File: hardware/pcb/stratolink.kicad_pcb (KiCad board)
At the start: 2 copper layers, 23.4 x 57.3 mm, 61 parts, among them J1 Solar panel direct solder, J2 Solar panel direct solder, J20 Conn_ARM_SWD_TagConnect_TC203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, J3 Conn_PinHeader_1x07_P2.54mm_V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, J4 Conn_PinHeader_1x07_P2.54mm_V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, U2 RAK3172, U5 TMP117NAIYBGR, U7 LIS2DH12TR

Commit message: Refine v1.1 ground zones and local pad connections
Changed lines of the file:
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@@
 			(pintype "power_in")
 			(solder_mask_margin 0)
+			(zone_connect 0)
 		)
 		(pad "6" smd roundrect
@@
 			(pintype "power_in")
 			(solder_mask_margin 0)
+			(zone_connect 0)
 		)
 		(pad "8" smd roundrect
@@
 			(pintype "power_in")
 			(solder_mask_margin 0)
+			(zone_connect 0)
 		)
 		(pad "9" smd roundrect
@@
 			(pinfunction "GND")
 			(pintype "power_in")
+			(zone_connect 2)
 		)
 		(pad "6" connect circle
@@
 			)
 		)
-	)
-	(zone
-		(net "GND")
-		(layer "B.Cu")
-		(hatch edge 0.5)
-		(connect_pads
-			(clearance 0.5)
-		)
-		(min_thickness 0.25)
-		(fill yes
-			(thermal_gap 0.5)
-			(thermal_bridge_width 0.5)
-			(island_removal_mode 0)
-		)
-		(polygon
-			(pts
-				(xy 52.941 29.045069) (xy 76.974 29.136) (xy 76.834 87.152) (xy 52.871 87.502)
-			)
-		)

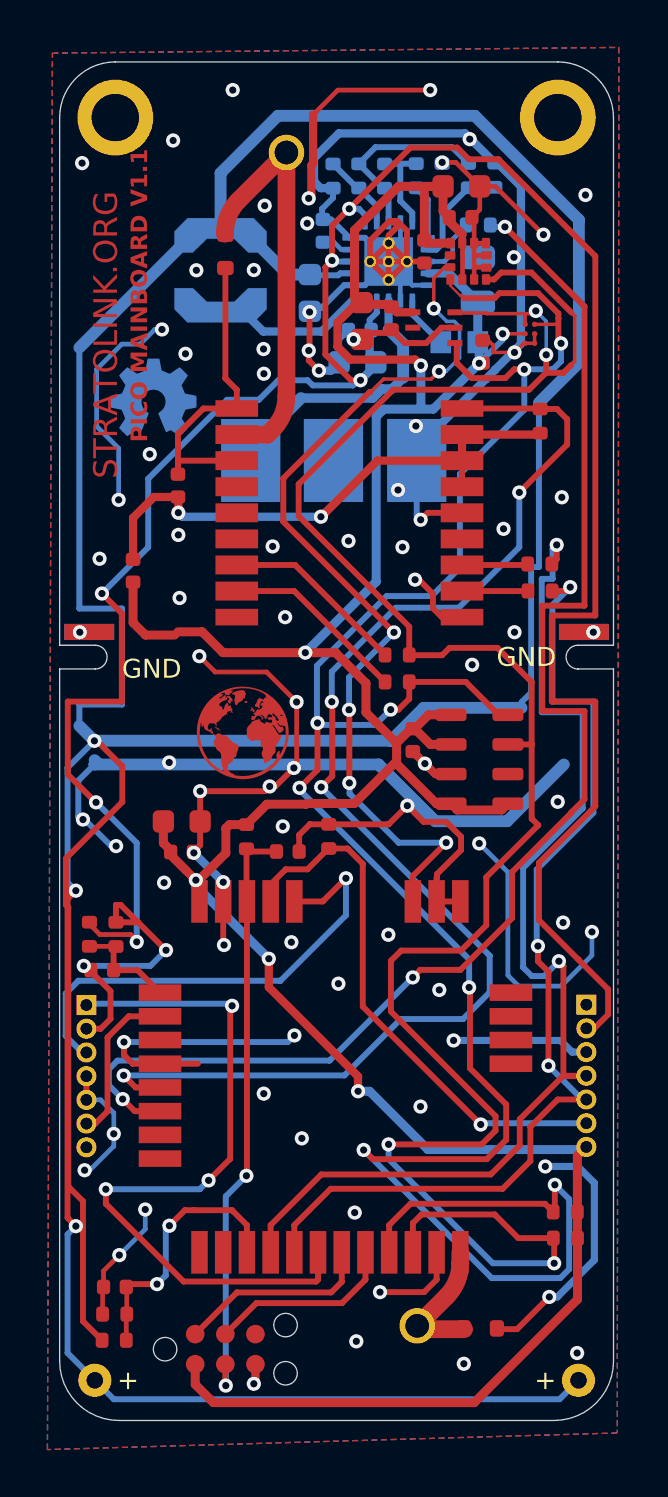
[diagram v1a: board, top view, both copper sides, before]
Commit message: Refine v1.1 edge routing and header pad rings
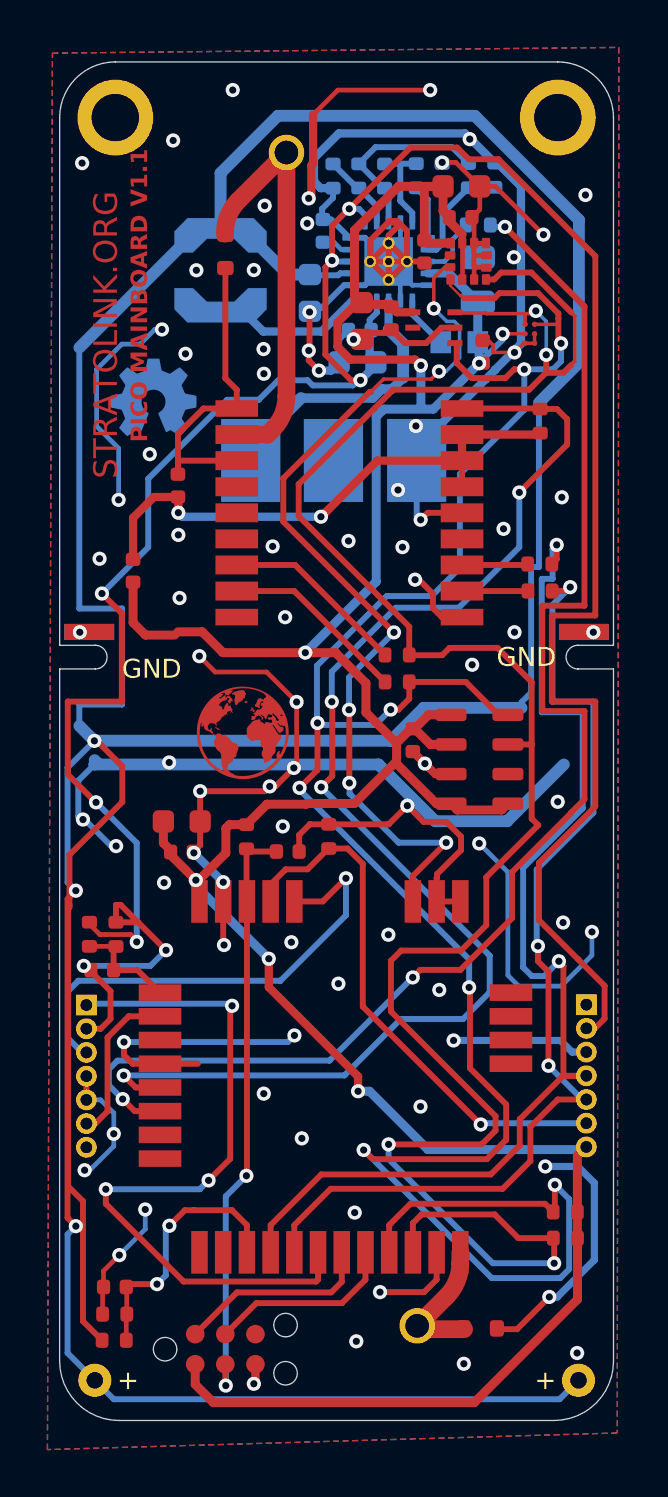
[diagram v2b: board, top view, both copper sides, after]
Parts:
- J3: footprint Connector_PinHeader_1.00mm:PinHeader_1x07_P1.00mm_Vertical -> lib:Stratolink_Header_Left_1x07_P1p00_D0p50_Pad0p88
- J4: footprint Connector_PinHeader_1.00mm:PinHeader_1x07_P1.00mm_Vertical -> lib:Stratolink_Header_Right_1x07_P1p00_D0p50_Pad0p88
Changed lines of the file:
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@@
 		)
 	)
-	(footprint "Connector_PinHeader_1.00mm:PinHeader_1x07_P1.00mm_Vertical"
+	(footprint "lib:Stratolink_Header_Right_1x07_P1p00_D0p50_Pad0p88"
 		(layer "F.Cu")
 		(at 75.531 69.158)
@@
 		(pad "1" thru_hole rect
 			(at 0 0)
-			(size 0.85 0.85)
+			(size 0.88 0.88)
 			(drill 0.5)
 			(layers "*.Cu" "*.Mask")
@@
 		(pad "2" thru_hole oval
 			(at 0 1)
-			(size 0.85 0.85)
+			(size 0.88 0.88)
 			(drill 0.5)
 			(layers "*.Cu" "*.Mask")
@@
 		(pad "3" thru_hole oval
 			(at 0 2)
-			(size 0.85 0.85)
+			(size 0.88 0.88)
 			(drill 0.5)
 			(layers "*.Cu" "*.Mask")
@@
 		(pad "4" thru_hole oval
 			(at 0 3)
-			(size 0.85 0.85)
+			(size 0.88 0.88)
 			(drill 0.5)
 			(layers "*.Cu" "*.Mask")
@@
 		(pad "5" thru_hole oval
 			(at 0 4)
-			(size 0.85 0.85)
+			(size 0.88 0.88)
 			(drill 0.5)
 			(layers "*.Cu" "*.Mask")
@@
 		(pad "6" thru_hole oval
 			(at 0 5)
-			(size 0.85 0.85)
+			(size 0.88 0.88)
 			(drill 0.5)
 			(layers "*.Cu" "*.Mask")
@@
 		(pad "7" thru_hole oval
 			(at 0 6)
-			(size 0.85 0.85)
+			(size 0.88 0.88)
 			(drill 0.5)
 			(layers "*.Cu" "*.Mask")
@@
 		)
 	)
-	(footprint "Connector_PinHeader_1.00mm:PinHeader_1x07_P1.00mm_Vertical"
+	(footprint "lib:Stratolink_Header_Left_1x07_P1p00_D0p50_Pad0p88"
 		(layer "F.Cu")
 		(at 54.444998 69.173998)
@@
 		(pad "1" thru_hole rect
 			(at 0 0)
-			(size 0.85 0.85)
+			(size 0.88 0.88)
 			(drill 0.5)
 			(layers "*.Cu" "*.Mask")
@@
 		(pad "2" thru_hole oval
 			(at 0 1.000001)
-			(size 0.85 0.85)
+			(size 0.88 0.88)
 			(drill 0.5)
 			(layers "*.Cu" "*.Mask")
@@
 		(pad "3" thru_hole oval
 			(at 0.000001 2.000003)
-			(size 0.85 0.85)
+			(size 0.88 0.88)
 			(drill 0.5)
 			(layers "*.Cu" "*.Mask")
@@
 		(pad "4" thru_hole oval
 			(at 0.000002 3.000002)
-			(size 0.85 0.85)
+			(size 0.88 0.88)
 			(drill 0.5)
 			(layers "*.Cu" "*.Mask")
@@
 		(pad "5" thru_hole oval
 			(at 0 4)
-			(size 0.85 0.85)
+			(size 0.88 0.88)
 			(drill 0.5)
 			(layers "*.Cu" "*.Mask")
@@
 		(pad "6" thru_hole oval
 			(at 0 5)
-			(size 0.85 0.85)
+			(size 0.88 0.88)
 			(drill 0.5)
 			(layers "*.Cu" "*.Mask")
@@
 		(pad "7" thru_hole oval
 			(at 0 6)
-			(size 0.85 0.85)
+			(size 0.88 0.88)
 			(drill 0.5)
 			(layers "*.Cu" "*.Mask")
@@
 	)
 	(segment
-		(start 53.580921 64.947713)
-		(end 53.580921 62.991411)
+		(start 53.73 64.947713)
+		(end 53.73 62.842332)
 		(width 0.25)
 		(layer "F.Cu")
@@
 	)
 	(segment
-		(start 53.580921 62.991411)
+		(start 53.73 65.049963)
+		(end 53.675 65.104963)
+		(width 0.25)
+		(layer "F.Cu")
+		(net "+SOLAR")
+	)
+	(segment
+		(start 53.73 62.842332)
 		(end 55.961085 60.611247)
 		(width 0.25)
@@
 	)
 	(segment
-		(start 53.683171 65.049963)
-		(end 53.580921 64.947713)
+		(start 53.73 65.049963)
+		(end 53.73 64.947713)
 		(width 0.25)
 		(layer "F.Cu")
@@
 	)
 	(segment
-		(start 53.683171 76.828171)
-		(end 53.683171 65.049963)
+		(start 53.675 76.82)
+		(end 53.675 65.104963)
 		(width 0.25)
 		(layer "F.Cu")
@@
 	(segment
 		(start 54.301 77.446)
-		(end 53.683171 76.828171)
+		(end 53.675 76.82)
 		(width 0.25)
 		(layer "F.Cu")
@@
 	)
 	(segment
-		(start 76.449 68.511)
-		(end 76.449 69.573097)
+		(start 76.299 68.361)
+		(end 76.299 69.75)
 		(width 0.25)
 		(layer "F.Cu")
@@
 	)
 	(segment
-		(start 75.864097 70.158)
+		(start 75.891 70.158)
 		(end 75.531 70.158)
 		(width 0.25)
@@
 	(segment
 		(start 75.187 67.249)
-		(end 76.449 68.511)
+		(end 76.299 68.361)
 		(width 0.25)
 		(layer "F.Cu")
@@
 	)
 	(segment
-		(start 76.449 69.573097)
-		(end 75.864097 70.158)
+		(start 76.299 69.75)
+		(end 75.891 70.158)
 		(width 0.25)
 		(layer "F.Cu")
@@
 	(segment
 		(start 54.267917 71.174001)
-		(end 53.57 70.476084)
+		(end 53.675 70.581084)
 		(width 0.25)
 		(layer "B.Cu")
@@
 	)
 	(segment
-		(start 53.57 70.476084)
-		(end 53.57 68.69)
+		(start 53.675 70.581084)
+		(end 53.675 68.584999)
 		(width 0.25)
 		(layer "B.Cu")
@@
 	)
 	(segment
-		(start 53.57 68.69)
+		(start 53.675 68.584999)
 		(end 54.111648 68.148353)
 		(width 0.25)

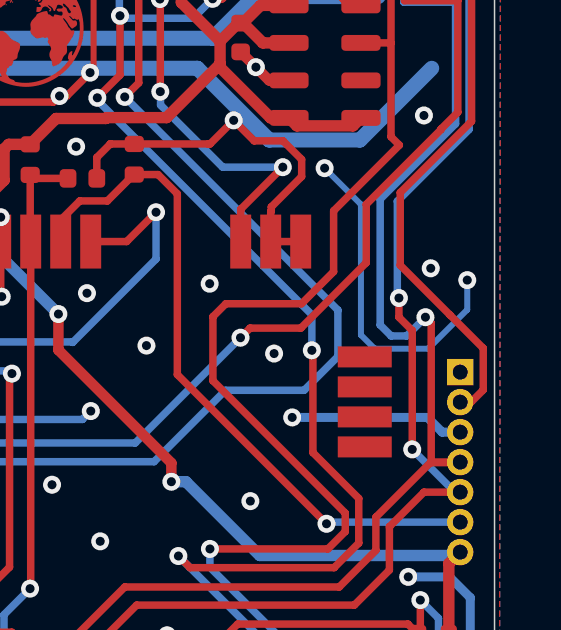
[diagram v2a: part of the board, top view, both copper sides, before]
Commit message: Use bare board finish and correct wire antenna assemblies
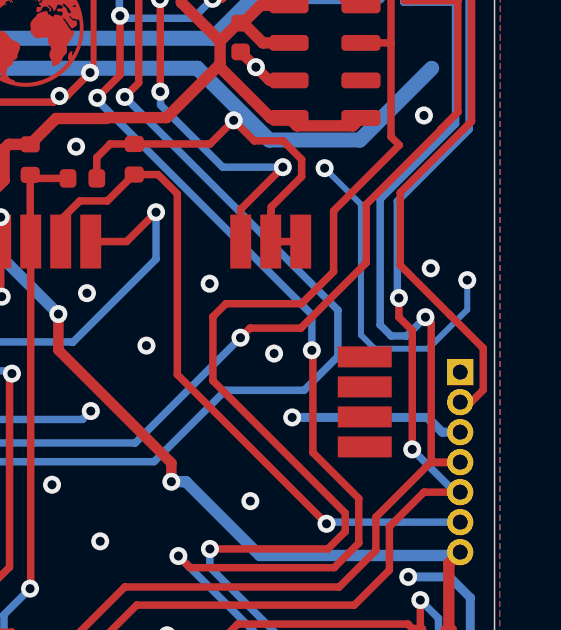
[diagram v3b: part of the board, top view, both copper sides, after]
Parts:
- AE1: value Antenna -> Enameled Cu wire 82mm (915MHz reference); footprint lib:4269 -> lib:Stratolink_LoRa_Wire_PTH_D1p0
- AE2: value Antenna -> Enameled Cu wire 48mm (GNSS L1); footprint lib:4269 -> lib:Stratolink_GNSS_Wire_PTH_D1p0
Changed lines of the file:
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@@
 			(layer "F.Mask"
 				(type "Top Solder Mask")
-				(thickness 0.01)
+				(thickness 0)
 			)
 			(layer "F.Cu"
@@
 			(layer "dielectric 1"
 				(type "core")
-				(thickness 0.31)
+				(thickness 0.33)
 				(material "FR4")
 				(epsilon_r 4.5)
@@
 			(layer "B.Mask"
 				(type "Bottom Solder Mask")
-				(thickness 0.01)
+				(thickness 0)
 			)
 			(layer "B.Paste"
@@
 		(allow_soldermask_bridges_in_footprints no)
 		(tenting
-			(front yes)
-			(back yes)
+			(front no)
+			(back no)
 		)
 		(covering
@@
 		)
 	)
-	(footprint "lib:4269"
+	(footprint "lib:Stratolink_GNSS_Wire_PTH_D1p0"
 		(layer "F.Cu")
 		(at 62.882 33.218 90)
-		(descr "4269-2")
+		(descr "Hand-formed enamelled copper wire; 48 mm from feed for GNSS L1; diameter not yet measured")
 		(tags "Antenna")
 		(property "Reference" "AE2"
@@
 			)
 		)
-		(property "Value" "Antenna"
+		(property "Value" "Enameled Cu wire 48mm (GNSS L1)"
 			(at 7.875 0 90)
 			(layer "F.SilkS")
@@
 			)
 		)
-		(property "Datasheet" "https://www.lcsc.com/product-detail/C89334.html?s_z=n_Johanson%25201575AT43A40"
+		(property "Datasheet" "https://stratolink.org/docs/hardware#antennas-and-suspension"
 			(at 0 0 90)
 			(layer "F.Fab")
@@
 			)
 		)
-		(property "Description" "2450AT18A100E"
+		(property "Description" "Hand-formed enamelled copper wire; 48 mm from feed for GNSS L1; diameter not yet measured"
 			(at 0 0 90)
 			(layer "F.Fab")
@@
 		(attr through_hole)
 		(duplicate_pad_numbers_are_jumpers no)
-		(fp_line
-			(start 17.5 -3.75)
-			(end 17.500001 3.749999)
-			(stroke
-				(width 0.1)
-				(type solid)
-			)
-			(layer "F.CrtYd")
-		)
-		(fp_line
-			(start -1.750001 -3.75)
-			(end 17.5 -3.75)
-			(stroke
-				(width 0.1)
-				(type solid)
-			)
-			(layer "F.CrtYd")
-		)
-		(fp_line
-			(start 17.500001 3.749999)
-			(end -1.75 3.750001)
-			(stroke
-				(width 0.1)
-				(type solid)
-			)
-			(layer "F.CrtYd")
-		)
-		(fp_line
-			(start -1.75 3.750001)
-			(end -1.750001 -3.75)
-			(stroke
-				(width 0.1)
-				(type solid)
-			)
-			(layer "F.CrtYd")
-		)
-		(fp_line
-			(start 4.5 -2.75)
-			(end 16.500001 -2.749999)
-			(stroke
-				(width 0.2)
-				(type solid)
-			)
-			(layer "F.Fab")
-		)
-		(fp_line
-			(start 16.500001 -2.749999)
-			(end 16.5 2.750001)
-			(stroke
-				(width 0.2)
-				(type solid)
-			)
-			(layer "F.Fab")
-		)
-		(fp_line
-			(start 0 0)
-			(end 4.5 0)
-			(stroke
-				(width 0.8)
-				(type solid)
-			)
-			(layer "F.Fab")
-		)
-		(fp_line
-			(start 4.5 2.75)
-			(end 4.5 -2.75)
-			(stroke
-				(width 0.2)
-				(type solid)
-			)
-			(layer "F.Fab")
-		)
-		(fp_line
-			(start 16.5 2.750001)
-			(end 4.5 2.75)
-			(stroke
-				(width 0.2)
-				(type solid)
-			)
-			(layer "F.Fab")
-		)
 		(pad "1" thru_hole circle
 			(at 0 0 90)
@@
 		)
 		(embedded_fonts no)
-		(model "${KIPRJMOD}/lib/gps.step"
+		(model "${KIPRJMOD}/lib/Stratolink_Wire_48mm_D0p321_Nominal.step"
 			(offset
 				(xyz 0 -0.2 0.15)
@@
 			)
 		)
-	)
+	(fp_line (start -1.25 -1.25) (end 49 -1.25) (stroke (width 0.05) (type solid)) (layer "F.CrtYd"))
+	(fp_line (start 49 -1.25) (end 49 1.25) (stroke (width 0.05) (type solid)) (layer "F.CrtYd"))
+	(fp_line (start 49 1.25) (end -1.25 1.25) (stroke (width 0.05) (type solid)) (layer "F.CrtYd"))
+	(fp_line (start -1.25 1.25) (end -1.25 -1.25) (stroke (width 0.05) (type solid)) (layer "F.CrtYd"))
+	(fp_line (start 0 0) (end 48 0) (stroke (width 0.321) (type solid)) (layer "F.Fab"))
+)
 	(footprint "lib:SMD6_LTR-390UV-01_LTO-L"
 		(layer "F.Cu")
@@
 		(embedded_fonts no)
 	)
-	(footprint "lib:4269"
+	(footprint "lib:Stratolink_LoRa_Wire_PTH_D1p0"
 		(layer "F.Cu")
 		(at 68.396 82.703 -90)
-		(descr "4269-2")
+		(descr "Hand-formed enamelled copper wire; 82 mm from feed for 915 MHz, 83 mm compromise or 86 mm for 868 MHz; diameter not yet measured")
 		(tags "Antenna")
 		(property "Reference" "AE1"
@@
 			)
 		)
-		(property "Value" "Antenna"
+		(property "Value" "Enameled Cu wire 82mm (915MHz reference)"
 			(at 7.875 0 90)
 			(layer "F.SilkS")
@@
 			)
 		)
-		(property "Datasheet" "https://www.digikey.com/en/products/detail/adafruit-industries-llc/4269/10313908"
+		(property "Datasheet" "https://stratolink.org/docs/hardware#antennas-and-suspension"
 			(at 0 0 90)
 			(layer "F.Fab")
@@
 			)
 		)
-		(property "Description" "1528-4269-ND"
+		(property "Description" "Hand-formed enamelled copper wire; 82 mm from feed for 915 MHz, 83 mm compromise or 86 mm for 868 MHz; diameter not yet measured"
 			(at 0 0 90)
 			(layer "F.Fab")
@@
 		(attr through_hole)
 		(duplicate_pad_numbers_are_jumpers no)
-		(fp_line
-			(start -1.750001 3.750001)
-			(end -1.750001 -3.75)
-			(stroke
-				(width 0.1)
-				(type solid)
-			)
-			(layer "F.CrtYd")
-		)
-		(fp_line
-			(start 17.500001 3.749999)
-			(end -1.750001 3.750001)
-			(stroke
-				(width 0.1)
-				(type solid)
-			)
-			(layer "F.CrtYd")
-		)
-		(fp_line
-			(start -1.750001 -3.75)
-			(end 17.5 -3.75)
-			(stroke
-				(width 0.1)
-				(type solid)
-			)
-			(layer "F.CrtYd")
-		)
-		(fp_line
-			(start 17.5 -3.75)
-			(end 17.500001 3.749999)
-			(stroke
-				(width 0.1)
-				(type solid)
-			)
-			(layer "F.CrtYd")
-		)
-		(fp_line
-			(start 4.5 2.75)
-			(end 4.5 -2.75)
-			(stroke
-				(width 0.2)
-				(type solid)
-			)
-			(layer "F.Fab")
-		)
-		(fp_line
-			(start 16.499998 2.75)
-			(end 4.5 2.75)
-			(stroke
-				(width 0.2)
-				(type solid)
-			)
-			(layer "F.Fab")
-		)
-		(fp_line
-			(start 0 0)
-			(end 4.5 0)
-			(stroke
-				(width 0.8)
-				(type solid)
-			)
-			(layer "F.Fab")
-		)
-		(fp_line
-			(start 16.500001 -2.749999)
-			(end 16.499998 2.75)
-			(stroke
-				(width 0.2)
-				(type solid)
-			)
-			(layer "F.Fab")
-		)
-		(fp_line
-			(start 4.5 -2.75)
-			(end 16.500001 -2.749999)
-			(stroke
-				(width 0.2)
-				(type solid)
-			)
-			(layer "F.Fab")
-		)
 		(pad "1" thru_hole circle
 			(at 0 0 270)
@@
 		)
 		(embedded_fonts no)
-		(model "${KIPRJMOD}/lib/gps.step"
+		(model "${KIPRJMOD}/lib/Stratolink_Wire_82mm_D0p321_Nominal.step"
 			(offset
 				(xyz 0 0 0)
@@
 			)
 		)
-	)
+	(fp_line (start -1.25 -1.25) (end 87 -1.25) (stroke (width 0.05) (type solid)) (layer "F.CrtYd"))
+	(fp_line (start 87 -1.25) (end 87 1.25) (stroke (width 0.05) (type solid)) (layer "F.CrtYd"))
+	(fp_line (start 87 1.25) (end -1.25 1.25) (stroke (width 0.05) (type solid)) (layer "F.CrtYd"))
+	(fp_line (start -1.25 1.25) (end -1.25 -1.25) (stroke (width 0.05) (type solid)) (layer "F.CrtYd"))
+	(fp_line (start 0 0) (end 82 0) (stroke (width 0.321) (type solid)) (layer "F.Fab"))
+)
 	(footprint "Resistor_SMD:R_0402_1005Metric"
 		(layer "F.Cu")
@@
 	)
 	(segment
-		(start 75.187 67.249)
-		(end 75.195 67.257)
-		(width 0.25)
-		(layer "F.Cu")
-		(net "VSTOR")
-	)
-	(segment
 		(start 71.824 33.503)
 		(end 75.909911 37.588911)
@@
 	)
 	(embedded_fonts no)
+	(gr_rect
+		(start 52 28)
+		(end 78 88)
+		(stroke
+			(width 0)
+			(type default)
+		)
+		(fill yes)
+		(locked yes)
+		(layer "F.Mask")
+	)
+	(gr_rect
+		(start 52 28)
+		(end 78 88)
+		(stroke
+			(width 0)
+			(type default)
+		)
+		(fill yes)
+		(locked yes)
+		(layer "B.Mask")
+	)
 )
